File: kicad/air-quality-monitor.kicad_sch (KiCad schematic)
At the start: 8 parts, among them J1 Conn_02x02_Top_Bottom, U1 SCD40-D-R2, U2 ESP32-C6-MINI-1

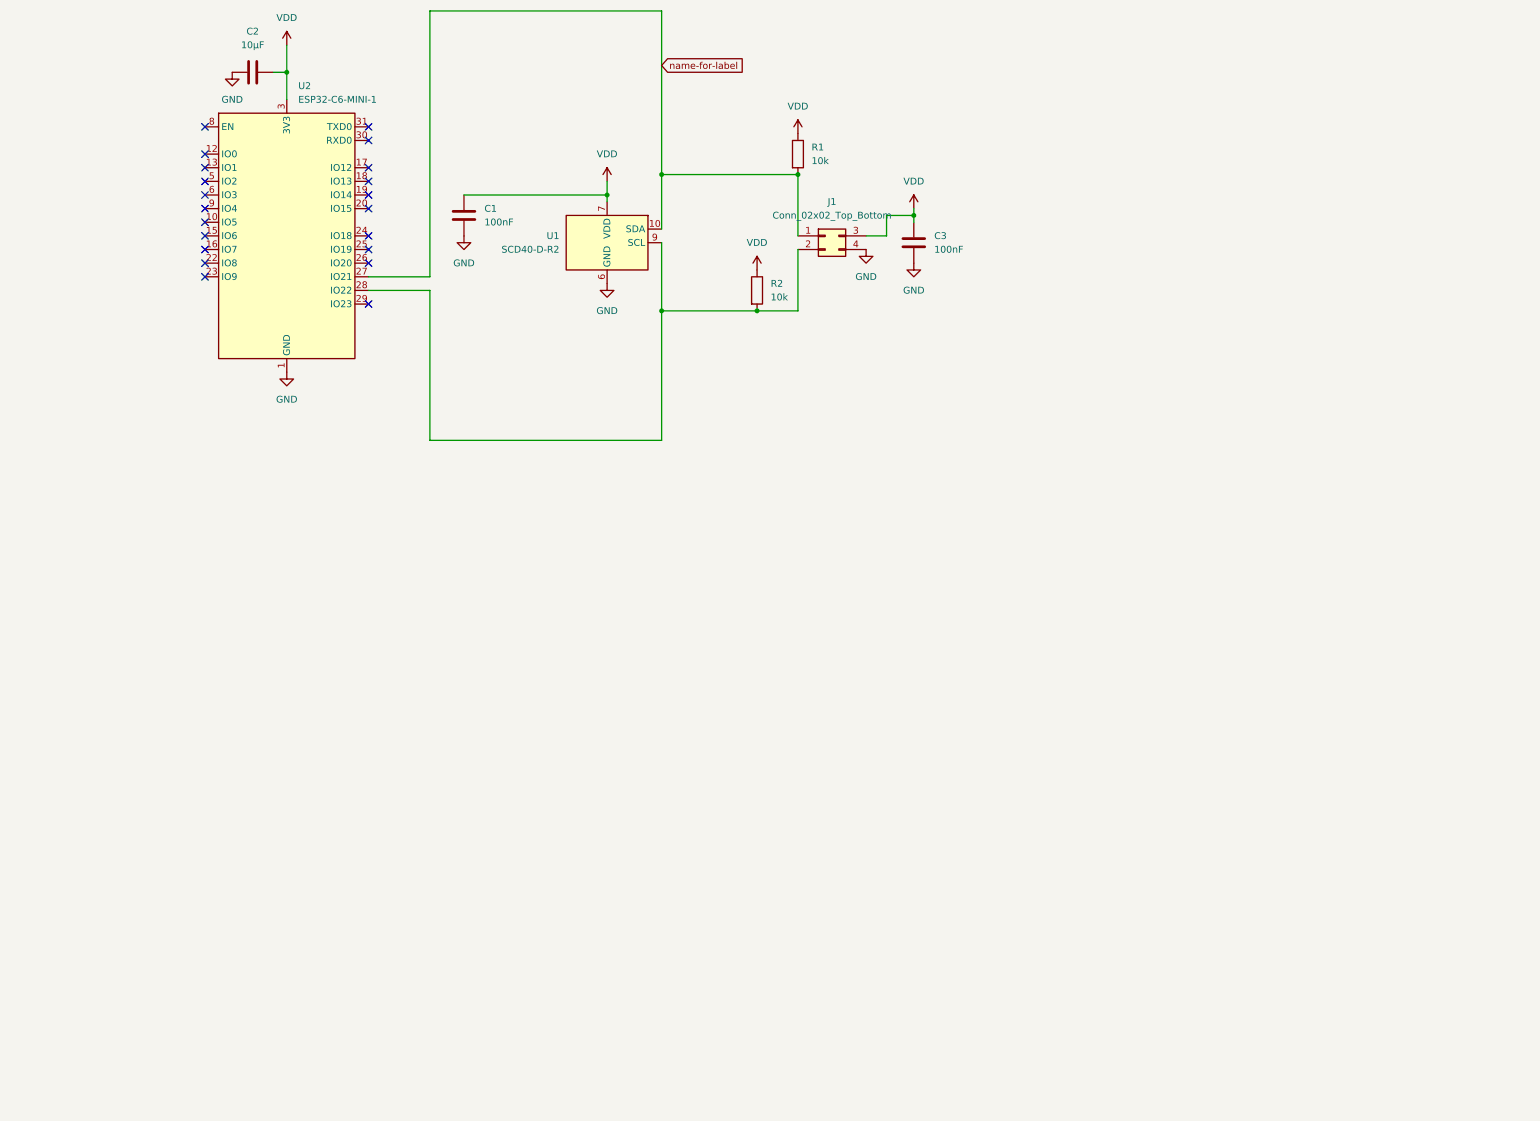
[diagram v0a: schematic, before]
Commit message: Draw the v1 schematic from the draft design
Replaces the placeholder (bare SCD40 chip, ESP32-C6-MINI-1, which can't be
hand-soldered) with the parts decided in kicad/README.md. KiCad has no
DevKitC-1 part, so the project library carries its symbol and footprint,
taken from Espressif's pin list and dimension drawing v1.2. ERC is clean.

Co-Authored-By: Claude Opus 5.5 <noreply@anthropic.com>
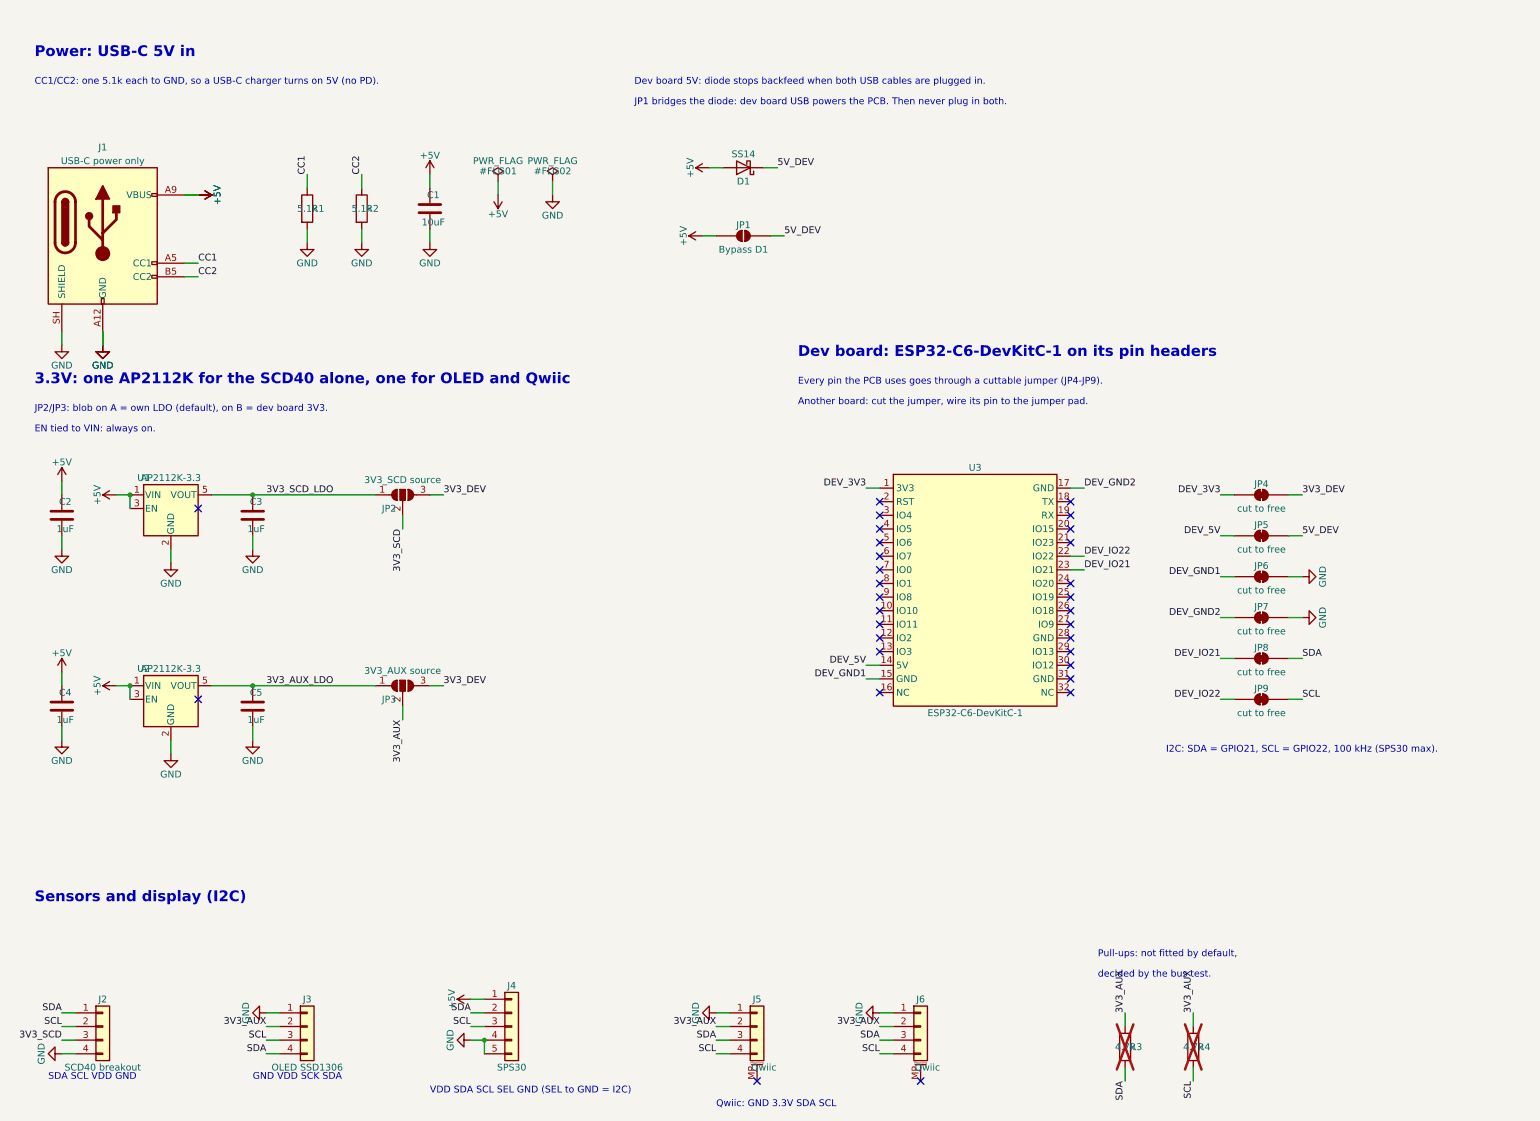
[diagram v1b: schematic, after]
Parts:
- removed J1: Conn_02x02_Top_Bottom, Connector_PinHeader_2.54mm:PinHeader_2x02_P2.54mm_Vertical, symbol Connector_Generic:Conn_02x02_Top_Bottom
- removed U1: SCD40-D-R2, Sensor:Sensirion_SCD4x-1EP_10.1x10.1mm_P1.25mm_EP4.8x4.8mm, symbol Sensor_Gas:SCD40-D-R2
- removed U2: ESP32-C6-MINI-1, RF_Module:ESP32-C6-MINI-1, symbol RF_Module:ESP32-C6-MINI-1
- added C4, C5: 1uF, Capacitor_SMD:C_0805_2012Metric_Pad1.18x1.45mm_HandSolder, symbol Device:C
- added D1: SS14, Diode_SMD:D_SMA, symbol Device:D_Schottky
- added J1: USB-C power only, Connector_USB:USB_C_Receptacle_GCT_USB4125-xx-x_6P_TopMnt_Horizontal, symbol Connector:USB_C_Receptacle_PowerOnly_6P
- added J2: SCD40 breakout, Connector_PinHeader_2.54mm:PinHeader_1x04_P2.54mm_Vertical, symbol Connector_Generic:Conn_01x04
- added J3: OLED SSD1306, Connector_PinHeader_2.54mm:PinHeader_1x04_P2.54mm_Vertical, symbol Connector_Generic:Conn_01x04
- added J4: SPS30, Connector_JST:JST_ZH_B5B-ZR_1x05_P1.50mm_Vertical, symbol Connector_Generic:Conn_01x05
- added J5, J6: Qwiic, Connector_JST:JST_SH_SM04B-SRSS-TB_1x04-1MP_P1.00mm_Horizontal, symbol Connector_Generic_MountingPin:Conn_01x04_MountingPin
- added JP1: Bypass D1, Jumper:SolderJumper-2_P1.3mm_Open_RoundedPad1.0x1.5mm, symbol Jumper:SolderJumper_2_Open
- added JP2: 3V3_SCD source, Jumper:SolderJumper-3_P1.3mm_Open_RoundedPad1.0x1.5mm_NumberLabels, symbol Jumper:SolderJumper_3_Open
- added JP3: 3V3_AUX source, Jumper:SolderJumper-3_P1.3mm_Open_RoundedPad1.0x1.5mm_NumberLabels, symbol Jumper:SolderJumper_3_Open
- added JP4, JP5, JP6, JP7, JP8, JP9: cut to free, Jumper:SolderJumper-2_P1.3mm_Bridged_RoundedPad1.0x1.5mm, symbol Jumper:SolderJumper_2_Bridged
- added R3, R4: 4.7k, Resistor_SMD:R_0805_2012Metric_Pad1.20x1.40mm_HandSolder, symbol Device:R
- added U1, U2: AP2112K-3.3, Package_TO_SOT_SMD:SOT-23-5_HandSoldering, symbol Regulator_Linear:AP2112K-3.3
- added U3: ESP32-C6-DevKitC-1, air-quality-monitor:ESP32-C6-DevKitC-1, symbol air-quality-monitor:ESP32-C6-DevKitC-1
- C1: value 100nF -> 10uF; footprint Capacitor_SMD:C_0603_1608Metric_Pad1.08x0.95mm_HandSolder -> Capacitor_SMD:C_0805_2012Metric_Pad1.18x1.45mm_HandSolder
- C2: value 10µF -> 1uF; footprint Capacitor_SMD:C_0603_1608Metric_Pad1.08x0.95mm_HandSolder -> Capacitor_SMD:C_0805_2012Metric_Pad1.18x1.45mm_HandSolder
- C3: value 100nF -> 1uF; footprint Capacitor_SMD:C_0603_1608Metric_Pad1.08x0.95mm_HandSolder -> Capacitor_SMD:C_0805_2012Metric_Pad1.18x1.45mm_HandSolder
- R1, R2: value 10k -> 5.1k; footprint Resistor_SMD:R_0603_1608Metric_Pad0.98x0.95mm_HandSolder -> Resistor_SMD:R_0805_2012Metric_Pad1.20x1.40mm_HandSolder
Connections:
- net name-for-label is gone; now on net GND: R1.2
- net GND: now also R2.2, C4.2, C5.2, J1.A12 (GND), J1.B12 (GND), J1.SH (SHIELD), J2.4 (Pin_4), J3.1 (Pin_1), J4.4 (Pin_4), J4.5 (Pin_5), J5.1 (Pin_1), J6.1 (Pin_1), JP6.2 (B), JP7.2 (B), U1.2 (GND), U2.2 (GND)
- removed net VDD: C1.1, C2.1, C3.1, R1.1, R2.1
- new net +5V: C1.1, C2.1, C4.1, D1.2 (A), J1.A9 (VBUS), J1.B9 (VBUS), J4.1 (Pin_1), JP1.1 (A), U1.1 (VIN), U1.3 (EN), U2.1 (VIN), U2.3 (EN)
- new net 3V3_AUX: J3.2 (Pin_2), J5.2 (Pin_2), J6.2 (Pin_2), JP3.2 (C), R3.1, R4.1
- new net 3V3_AUX_LDO: C5.1, JP3.1 (A), U2.5 (VOUT)
- new net 3V3_DEV: JP2.3 (B), JP3.3 (B), JP4.2 (B)
- new net 3V3_SCD: J2.3 (Pin_3), JP2.2 (C)
- new net 3V3_SCD_LDO: C3.1, JP2.1 (A), U1.5 (VOUT)
- new net 5V_DEV: D1.1 (K), JP1.2 (B), JP5.2 (B)
- new net CC1: J1.A5 (CC1), R1.1
- new net CC2: J1.B5 (CC2), R2.1
- new net DEV_3V3: JP4.1 (A), U3.1 (3V3)
- new net DEV_5V: JP5.1 (A), U3.14 (5V)
- new net DEV_GND1: JP6.1 (A), U3.15 (GND)
- new net DEV_GND2: JP7.1 (A), U3.17 (GND)
- new net DEV_IO21: JP8.1 (A), U3.23 (IO21)
- new net DEV_IO22: JP9.1 (A), U3.22 (IO22)
- new net SCL: J2.2 (Pin_2), J3.3 (Pin_3), J4.3 (Pin_3), J5.4 (Pin_4), J6.4 (Pin_4), JP9.2 (B), R4.2
- new net SDA: J2.1 (Pin_1), J3.4 (Pin_4), J4.2 (Pin_2), J5.3 (Pin_3), J6.3 (Pin_3), JP8.2 (B), R3.2
- no-connect marks 21 -> 30
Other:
- note added: "3.3V: one AP2112K for the SCD40 alone, one for OLED and Qwiic"
- note added: "Another board: cut the jumper, wire its pin to the jumper pad."
- note added: "CC1/CC2: one 5.1k each to GND, so a USB-C charger turns on 5V (no PD)."
- note added: "Dev board 5V: diode stops backfeed when both USB cables are plugged in."
- note added: "Dev board: ESP32-C6-DevKitC-1 on its pin headers"
- note added: "EN tied to VIN: always on."
- note added: "Every pin the PCB uses goes through a cuttable jumper (JP4-JP9)."
- note added: "GND VDD SCK SDA"
- note added: "I2C: SDA = GPIO21, SCL = GPIO22, 100 kHz (SPS30 max)."
- note added: "JP1 bridges the diode: dev board USB powers the PCB. Then never plug in both."
- note added: "JP2/JP3: blob on A = own LDO (default), on B = dev board 3V3."
- note added: "Power: USB-C 5V in"
- note added: "Pull-ups: not fitted by default,"
- note added: "Qwiic: GND 3.3V SDA SCL"
- note added: "SDA SCL VDD GND"
- note added: "Sensors and display (I2C)"
- note added: "VDD SDA SCL SEL GND (SEL to GND = I2C)"
- note added: "decided by the bus test."
- title: (none) -> Air quality monitor
